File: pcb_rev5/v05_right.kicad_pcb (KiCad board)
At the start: 2 copper layers, 170.7 x 135.9 mm, 74 parts, among them SW1 SW_Push, U1 ProMicro

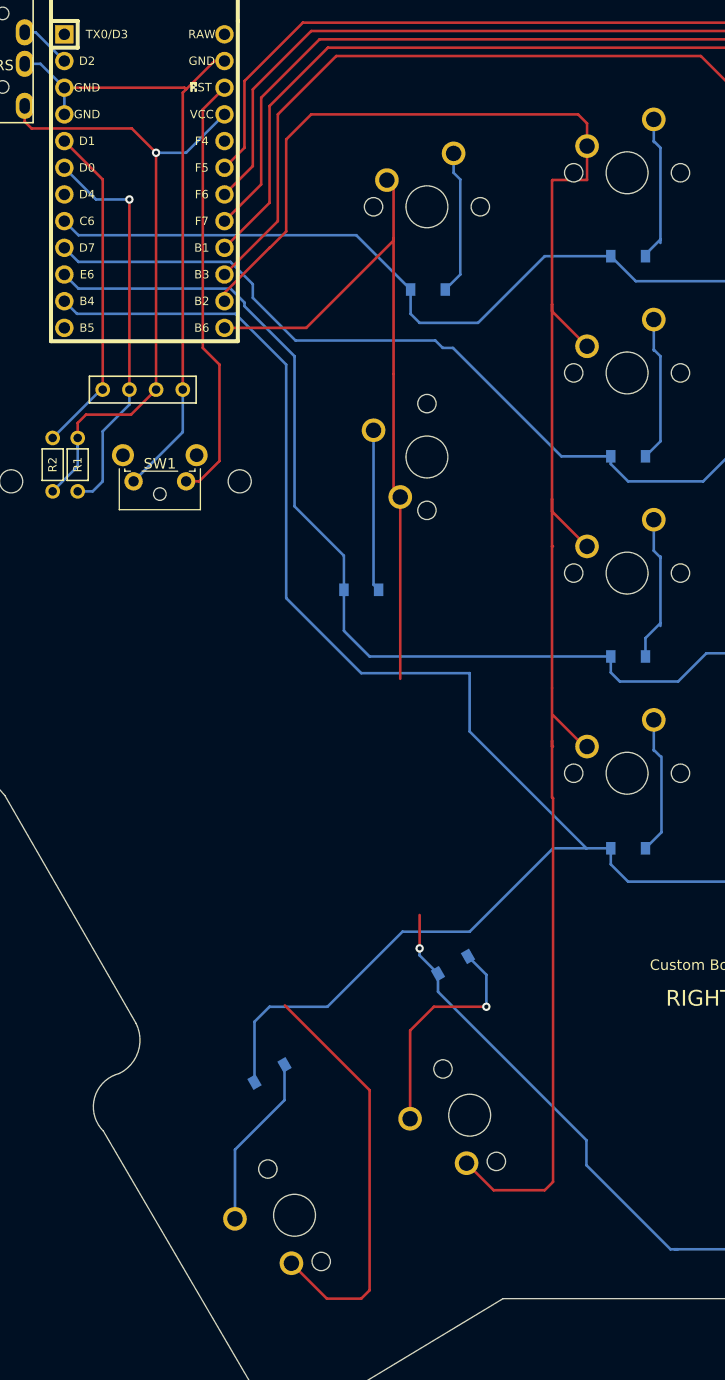
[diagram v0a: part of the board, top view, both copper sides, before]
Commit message: Modified right side: moved misc components under OLED cover, added keys in column 6
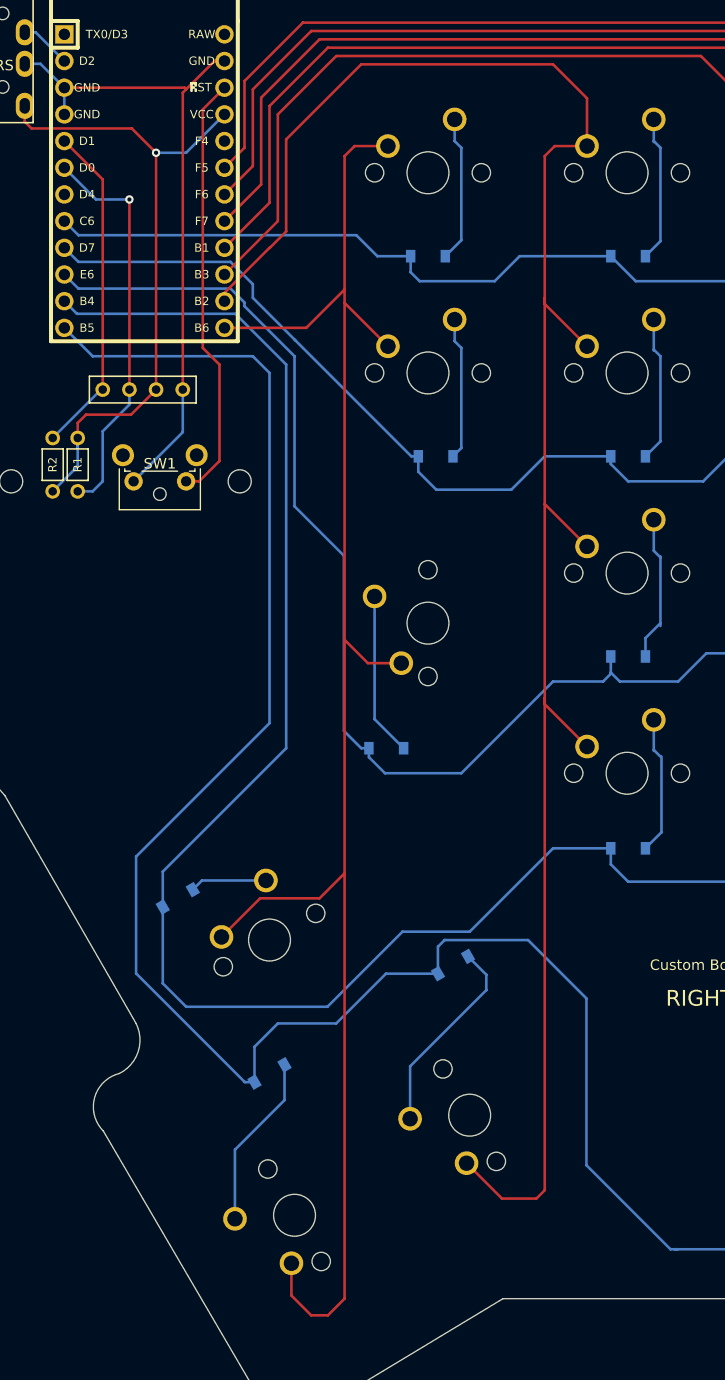
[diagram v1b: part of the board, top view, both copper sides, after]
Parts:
- added D16: D_Small, kbd:D_SOD-123, B.Cu at (-141.3, 67.5)
- added D46: D_Small, kbd:D_SOD-123, B.Cu at (-157.2, 126.2)
- added MX16: MX-NoLED, MX_Only:MXOnly-1U-NoLED, F.Cu at (-142.1, 59.5)
- added MX46: MX-NoLED, MX_Only:MXOnly-1.5U-NoLED, F.Cu at (-154.8, 139.7)
- moved MX36 26.3 mm to (-157.2, 113.5), turned to 30 degrees
- moved D36 18.8 mm to (-165.9, 109.5)
- moved MX26 15.8 mm to (-142.1, 83.3)
- moved D26 15.3 mm to (-146.1, 95.2)
- moved MX06 3.24 mm to (-142.1, 40.5)
- moved D06 3.17 mm to (-142.1, 48.4)
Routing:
- net row4: track 149.3 -> 277.0 mm, vias 1 -> 0
- net col6: track 108.2 -> 162.2 mm
- net Net-(D46-Pad2): track 0.00 -> 16.6 mm
- net row2: track 204.4 -> 219.2 mm
- net Net-(D16-Pad2): track 0.00 -> 13.6 mm
- net Net-(D36-Pad2): track 16.6 -> 7.32 mm
- net col5: track 178.1 -> 185.6 mm
- net row0: track 177.9 -> 174.2 mm
- net row1: track 180.2 -> 183.8 mm
- net row3: track 252.8 -> 255.9 mm
- net Net-(D45-Pad2): track 22.1 -> 19.2 mm, vias 1 -> 0
